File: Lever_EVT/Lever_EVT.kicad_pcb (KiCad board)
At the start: 2 copper layers, 150 x 174 mm, 28 parts, among them J106 Screw_Terminal_01x02, SW101 SW_SPDT_312, SW102 SW_SPDT_312

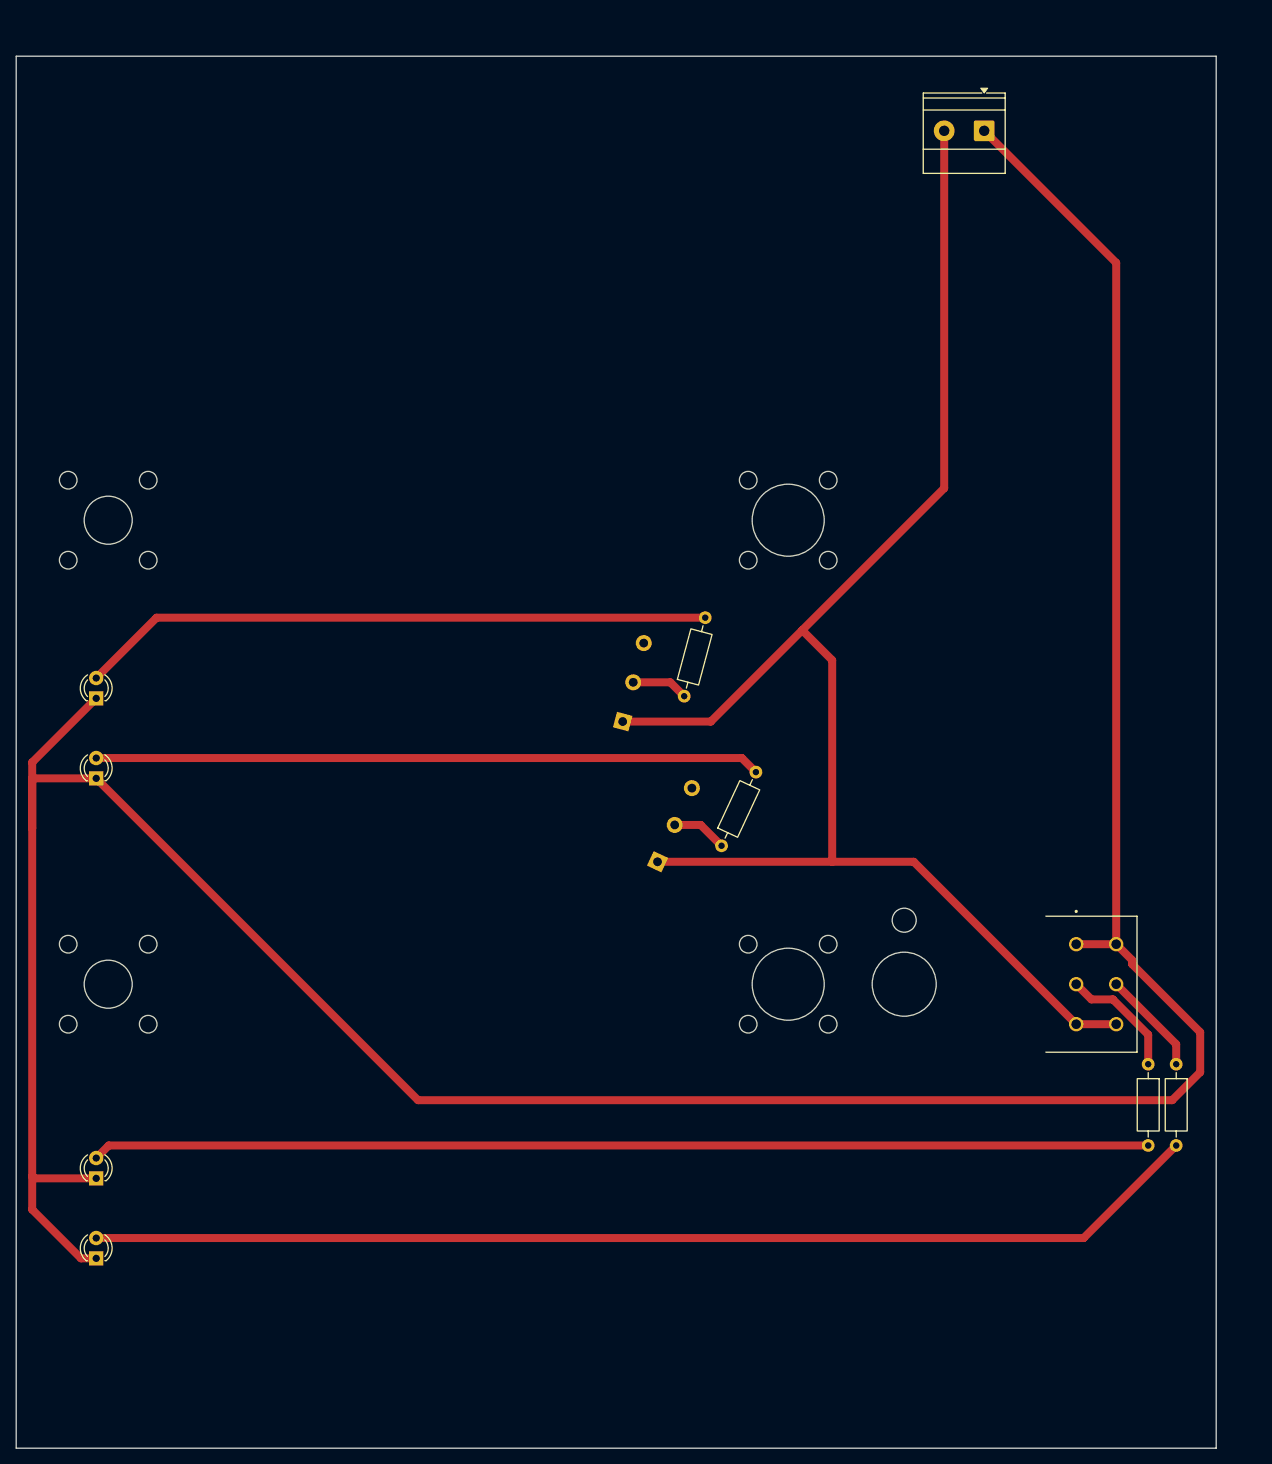
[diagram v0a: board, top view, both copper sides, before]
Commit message: add mounting holes
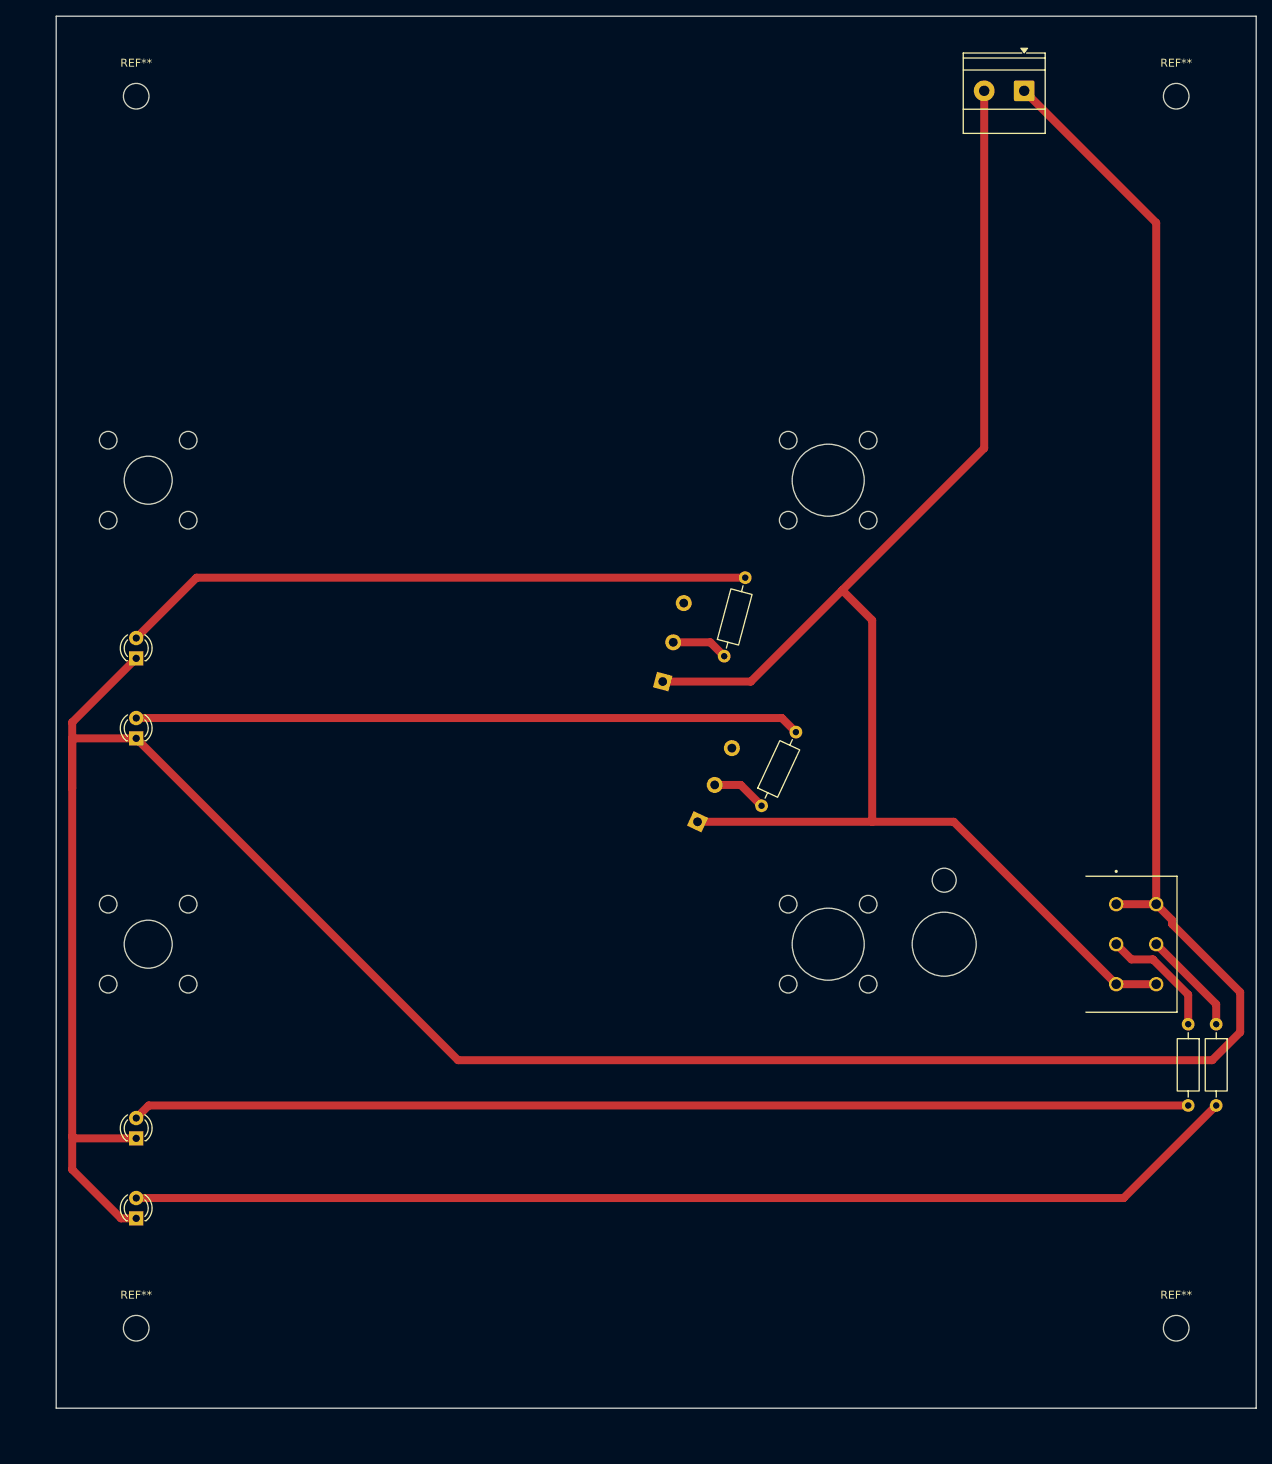
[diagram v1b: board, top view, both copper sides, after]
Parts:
- added REF**: MountingHole_3.2mm_M3, MountingHole:MountingHole_3.2mm_M3, F.Cu at (160.0, 26.0)
- added REF**: MountingHole_3.2mm_M3, MountingHole:MountingHole_3.2mm_M3, F.Cu at (30.0, 180.0)
- added REF**: MountingHole_3.2mm_M3, MountingHole:MountingHole_3.2mm_M3, F.Cu at (30.0, 26.0)
- added REF**: MountingHole_3.2mm_M3, MountingHole:MountingHole_3.2mm_M3, F.Cu at (160.0, 180.0)
- moved D101 7.07 mm to (30.0, 156.3)
- moved D102 7.07 mm to (30.0, 166.3)
- moved D103 7.07 mm to (30.0, 96.3)
- moved D104 7.07 mm to (30.0, 106.3)
- moved J106 7.07 mm to (141.0, 25.3)
- moved R101 7.07 mm to (152.5, 127.0)
- moved R102 7.07 mm to (161.5, 142.0)
- moved R103 7.07 mm to (103.5, 96.0)
- moved R104 7.07 mm to (165.0, 142.0)
- moved R105 7.07 mm to (108.2, 114.7)
- moved REF** 7.07 mm to (121.5, 79.0)
- moved REF** 7.07 mm to (36.5, 79.0)
- moved REF** 7.07 mm to (121.5, 127.0)
- moved REF** 7.07 mm to (36.5, 127.0)
- moved REF** 7.07 mm to (121.5, 137.0)
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
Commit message: user save
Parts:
- moved SW101 3.91 mm to (95.0, 103.0)
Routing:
- net Net-(D104-A): track 83.2 -> 87.7 mm
- net +5V: track 193.2 -> 195.6 mm
- net Net-(SW101-C): track 7.09 -> 8.05 mm
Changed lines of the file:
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@@
 	(footprint "Button_Switch_THT:SW_XKB_DM1-16UP-1"
 		(layer "B.Cu")
-		(at 95.8148 99.173097 75)
+		(at 95 103 75)
 		(descr "1A 30V SPDT Micro Switch rated for one million cycles, W12.7xD5.7xH6.6, https://www.helloxkb.com/public/images/pdf/DMX-XXXP-X.pdf")
 		(tags "SPDT endstop limit switch vertical hook lever XKB DM1-16UP-1")
@@
 	)
 	(segment
-		(start 110.702648 103.73)
+		(start 30.639 104.369)
+		(end 31.901 104.369)
+		(width 1)
+		(layer "F.Cu")
+		(net 5)
+	)
+	(segment
+		(start 30 103.73)
+		(end 30.639 104.369)
+		(width 1)
+		(layer "F.Cu")
+		(net 5)
+	)
+	(segment
+		(start 36.27 110)
+		(end 107.950754 110)
+		(width 1)
+		(layer "F.Cu")
+		(net 5)
+	)
+	(segment
+		(start 31.901 105.631)
+		(end 36.27 110)
+		(width 1)
+		(layer "F.Cu")
+		(net 5)
+	)
+	(segment
+		(start 31.901 104.369)
+		(end 31.901 105.631)
+		(width 1)
+		(layer "F.Cu")
+		(net 5)
+	)
+	(segment
+		(start 107.950754 110)
 		(end 112.461701 105.489053)
-		(width 1)
-		(layer "F.Cu")
-		(net 5)
-	)
-	(segment
-		(start 30 103.73)
-		(end 110.702648 103.73)
 		(width 1)
 		(layer "F.Cu")
@@
 	)
 	(segment
+		(start 101 101)
+		(end 102.826903 99.173097)
+		(width 1)
+		(layer "F.Cu")
+		(net 6)
+	)
+	(segment
+		(start 97 101)
+		(end 101 101)
+		(width 1)
+		(layer "F.Cu")
+		(net 6)
+	)
+	(segment
 		(start 136 70)
 		(end 136 25.3275)
@@
 	)
 	(segment
+		(start 102.826903 99.173097)
+		(end 106.826903 99.173097)
+		(width 1)
+		(layer "F.Cu")
+		(net 6)
+	)
+	(segment
 		(start 157.5 137)
 		(end 152.5 137)
@@
 	)
 	(segment
-		(start 95.8148 99.173097)
-		(end 106.826903 99.173097)
+		(start 95 103)
+		(end 97 101)
 		(width 1)
 		(layer "F.Cu")
@@
 	)
 	(segment
-		(start 101.766194 94.266194)
+		(start 96.3148 98.093097)
+		(end 97.407897 97)
+		(width 1)
+		(layer "F.Cu")
+		(net 9)
+	)
+	(segment
+		(start 97.407897 97)
+		(end 102.5 97)
+		(width 1)
+		(layer "F.Cu")
+		(net 9)
+	)
+	(segment
+		(start 102.5 97)
 		(end 103.5 96)
 		(width 1)
 		(layer "F.Cu")
-		(net 9)
-	)
-	(segment
-		(start 97.1296 94.266194)
-		(end 101.766194 94.266194)
-		(width 1)
-		(layer "F.Cu")

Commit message: user save
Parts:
- added G***: LOGO, LOGO, F.Cu at (31.7, 86.3)
- moved SW101 2.33 mm to (93.4, 101.3)
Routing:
- net Net-(SW101-C): track 8.05 -> 10.0 mm
- net +5V: track 195.6 -> 197.0 mm
- net Net-(D104-A): track 87.7 -> 86.7 mm

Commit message: user save
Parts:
- moved SW101 1.20 mm to (94.6, 101.3)
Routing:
- net +5V: track 197.0 -> 195.3 mm
- net Net-(SW101-C): track 10.0 -> 8.25 mm
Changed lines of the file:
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@@
 	(footprint "Button_Switch_THT:SW_XKB_DM1-16UP-1"
 		(layer "B.Cu")
-		(at 93.4 101.3 75)
+		(at 94.6 101.3 75)
 		(descr "1A 30V SPDT Micro Switch rated for one million cycles, W12.7xD5.7xH6.6, https://www.helloxkb.com/public/images/pdf/DMX-XXXP-X.pdf")
 		(tags "SPDT endstop limit switch vertical hook lever XKB DM1-16UP-1")
@@
 	)
 	(segment
+		(start 122 116.697141)
+		(end 100.167899 116.697141)
+		(width 1)
+		(layer "F.Cu")
+		(net 6)
+	)
+	(segment
+		(start 96.7 101.3)
+		(end 97 101)
+		(width 1)
+		(layer "F.Cu")
+		(net 6)
+	)
+	(segment
+		(start 136 70)
+		(end 136 25.3275)
+		(width 1)
+		(layer "F.Cu")
+		(net 6)
+	)
+	(segment
+		(start 101 101)
+		(end 102.826903 99.173097)
+		(width 1)
+		(layer "F.Cu")
+		(net 6)
+	)
+	(segment
+		(start 122 116.697141)
+		(end 122 91.5)
+		(width 1)
+		(layer "F.Cu")
+		(net 6)
+	)
+	(segment
+		(start 97 101)
+		(end 101 101)
+		(width 1)
+		(layer "F.Cu")
+		(net 6)
+	)
+	(segment
+		(start 122 91.5)
+		(end 118.25 87.75)
+		(width 1)
+		(layer "F.Cu")
+		(net 6)
+	)
+	(segment
+		(start 118.25 87.75)
+		(end 136 70)
+		(width 1)
+		(layer "F.Cu")
+		(net 6)
+	)
+	(segment
+		(start 94.6 101.3)
+		(end 96.7 101.3)
+		(width 1)
+		(layer "F.Cu")
+		(net 6)
+	)
+	(segment
+		(start 157.5 137)
+		(end 152.5 137)
+		(width 1)
+		(layer "F.Cu")
+		(net 6)
+	)
+	(segment
 		(start 106.826903 99.173097)
 		(end 118.25 87.75)
@@
 	)
 	(segment
-		(start 122 116.697141)
-		(end 100.167899 116.697141)
-		(width 1)
-		(layer "F.Cu")
-		(net 6)
-	)
-	(segment
-		(start 101 101)
-		(end 102.826903 99.173097)
-		(width 1)
-		(layer "F.Cu")
-		(net 6)
-	)
-	(segment
-		(start 93.4 101.3)
-		(end 93.4 100.9)
-		(width 1)
-		(layer "F.Cu")
-		(net 6)
-	)
-	(segment
-		(start 136 70)
-		(end 136 25.3275)
-		(width 1)
-		(layer "F.Cu")
-		(net 6)
-	)
-	(segment
-		(start 122 116.697141)
-		(end 122 91.5)
-		(width 1)
-		(layer "F.Cu")
-		(net 6)
-	)
-	(segment
-		(start 122 91.5)
-		(end 118.25 87.75)
-		(width 1)
-		(layer "F.Cu")
-		(net 6)
-	)
-	(segment
-		(start 118.25 87.75)
-		(end 136 70)
-		(width 1)
-		(layer "F.Cu")
-		(net 6)
-	)
-	(segment
-		(start 93.8 101.3)
-		(end 96.7 101.3)
-		(width 1)
-		(layer "F.Cu")
-		(net 6)
-	)
-	(segment
-		(start 157.5 137)
-		(end 152.5 137)
-		(width 1)
-		(layer "F.Cu")
-		(net 6)
-	)
-	(segment
-		(start 93.4 100.9)
-		(end 93.8 101.3)
-		(width 1)
-		(layer "F.Cu")
-		(net 6)
-	)
-	(segment
-		(start 96.7 101.3)
-		(end 97 101)
+		(start 132.197141 116.697141)
+		(end 122 116.697141)
 		(width 1)
 		(layer "F.Cu")
@@
 	)
 	(segment
-		(start 97 101)
-		(end 101 101)
-		(width 1)
-		(layer "F.Cu")
-		(net 6)
-	)
-	(segment
-		(start 132.197141 116.697141)
-		(end 122 116.697141)
-		(width 1)
-		(layer "F.Cu")
-		(net 6)
-	)
-	(segment
 		(start 154.401 133.901)
 		(end 152.5 132)
@@
 	)
 	(segment
+		(start 95.9148 96.393097)
+		(end 96.800994 96.393097)
+		(width 1)
+		(layer "F.Cu")
+		(net 9)
+	)
+	(segment
+		(start 97.407897 97)
+		(end 102.5 97)
+		(width 1)
+		(layer "F.Cu")
+		(net 9)
+	)
+	(segment
 		(start 96.800994 96.393097)
 		(end 97.407897 97)
@@
 	)
 	(segment
-		(start 94.7148 96.393097)
-		(end 94.7148 95.993097)
-		(width 1)
-		(layer "F.Cu")
-		(net 9)
-	)
-	(segment
-		(start 95.1148 96.393097)
-		(end 96.800994 96.393097)
-		(width 1)
-		(layer "F.Cu")
-		(net 9)
-	)
-	(segment
-		(start 94.7148 95.993097)
-		(end 95.1148 96.393097)
-		(width 1)
-		(layer "F.Cu")
-		(net 9)
-	)
-	(segment
 		(start 102.5 97)
 		(end 103.5 96)
 		(width 1)
 		(layer "F.Cu")
-		(net 9)
-	)
-	(segment
-		(start 97.407897 97)
-		(end 102.5 97)
-		(width 1)
-		(layer "F.Cu")
